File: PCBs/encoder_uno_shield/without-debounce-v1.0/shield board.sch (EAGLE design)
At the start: 13 parts, among them U1 ARDUINOR3-BPLACE

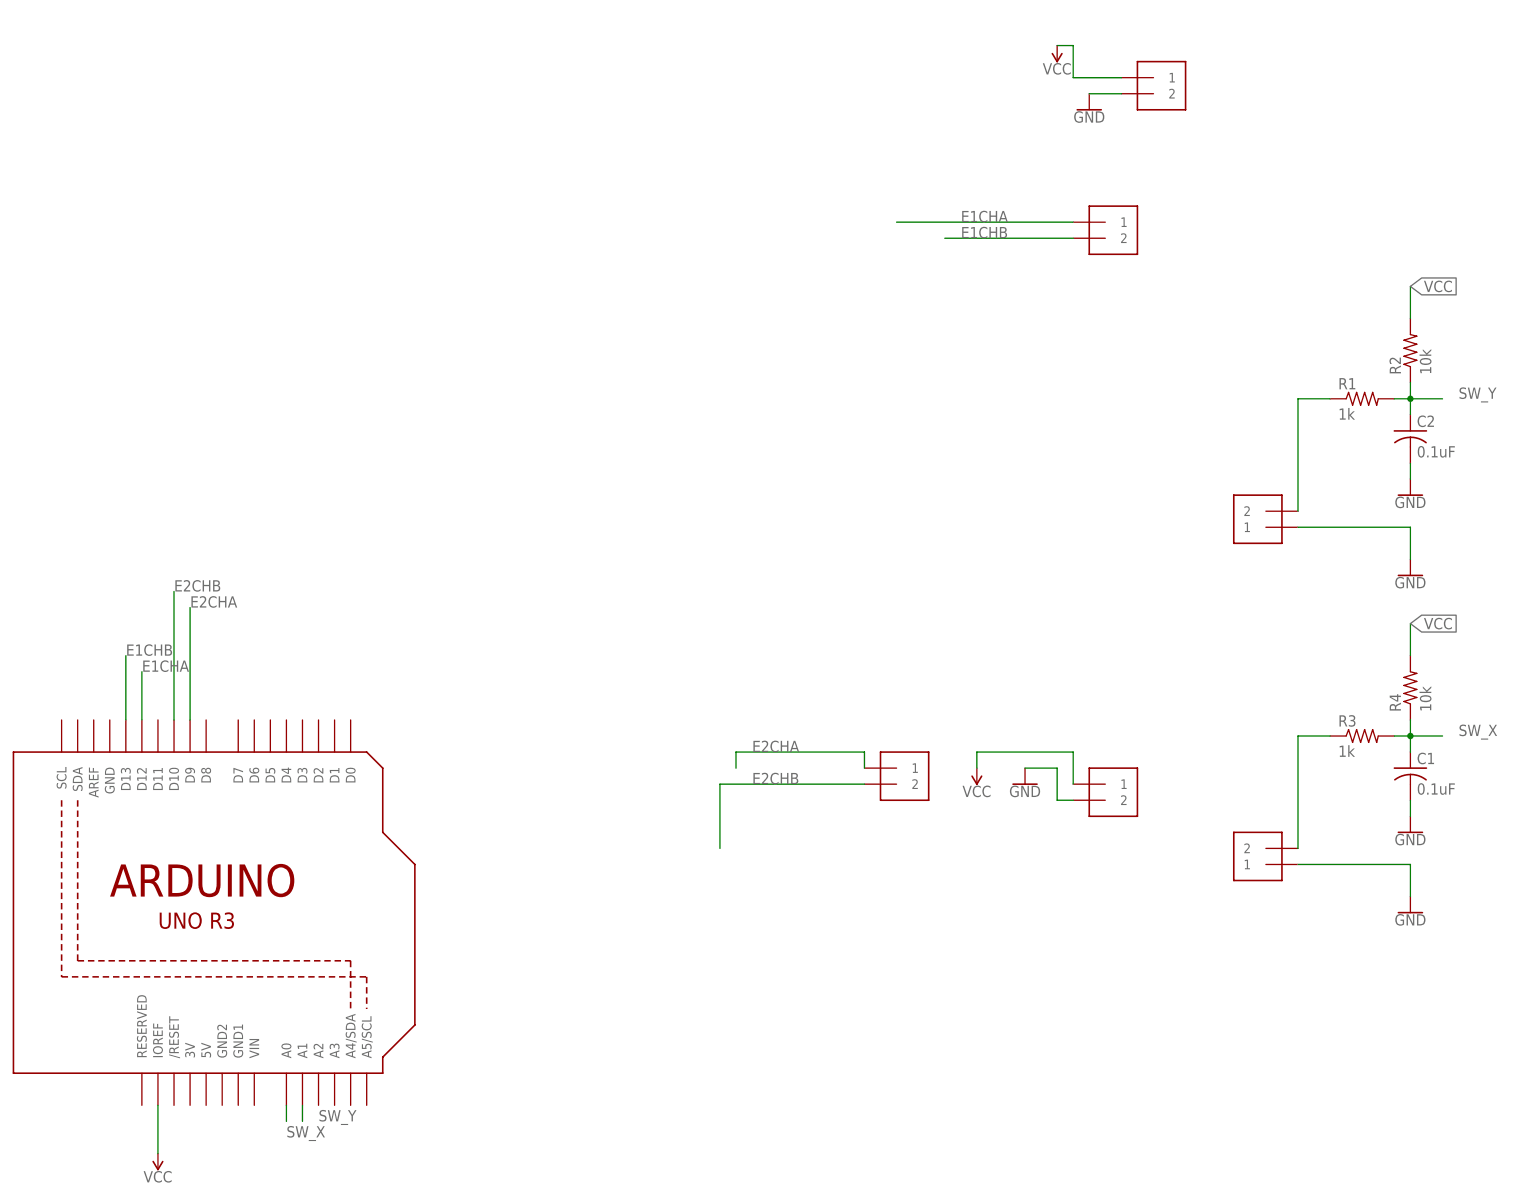
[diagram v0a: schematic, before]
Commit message: realized i only need one switch port, about to redesign
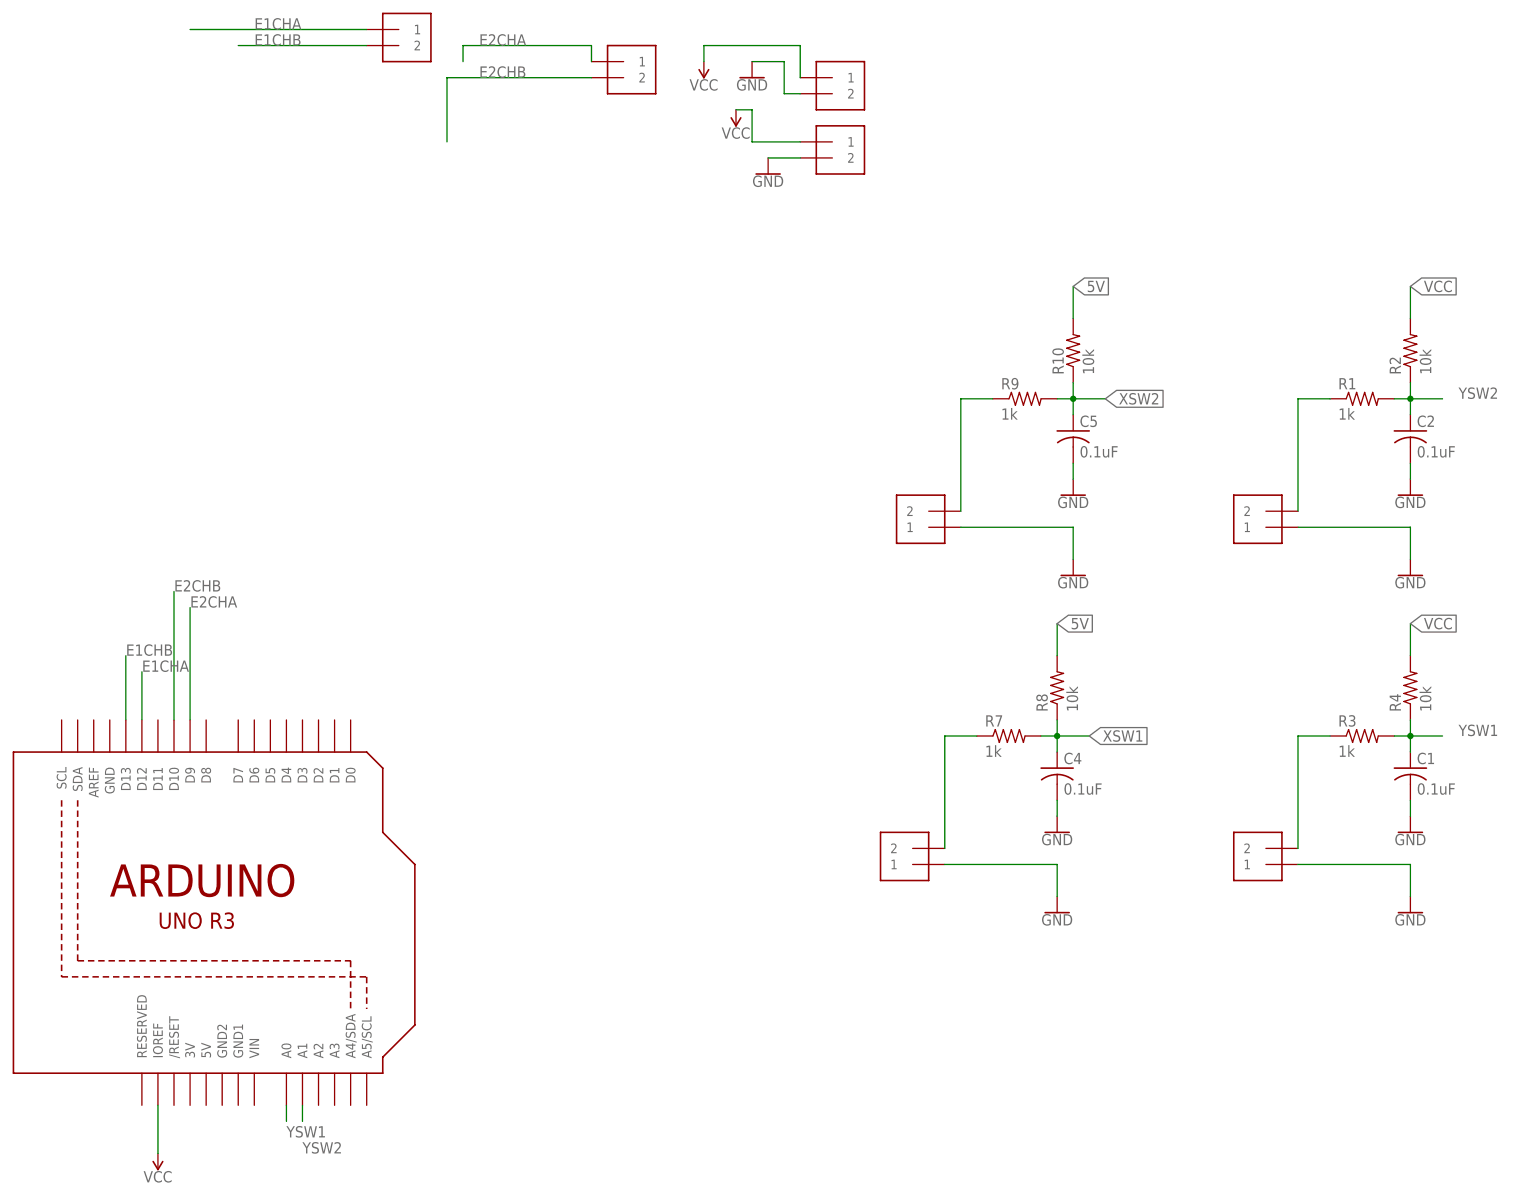
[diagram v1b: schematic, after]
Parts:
- added C4, C5: 0.1uF, adafruit:C-USC0603
- added R10, R8: 10k, resistor:R-US_R0603
- added R7, R9: 1k, resistor:R-US_R0603
- added U$7, U$8: MOLEX_0039301022, pat:MOLEX_0039301022
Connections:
- net SW_X renamed YSW1
- net SW_Y renamed YSW2
- new net 5V: R10.2, R8.2
- new net N$3: R7.1, U$7.2
- new net N$5: R9.1, U$8.2
- new net XSW1: C4.1, R7.2, R8.1
- new net XSW2: C5.1, R10.1, R9.2
- net GND: now also C4.2, C5.2, U$7.1, U$8.1

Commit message: routed new board design
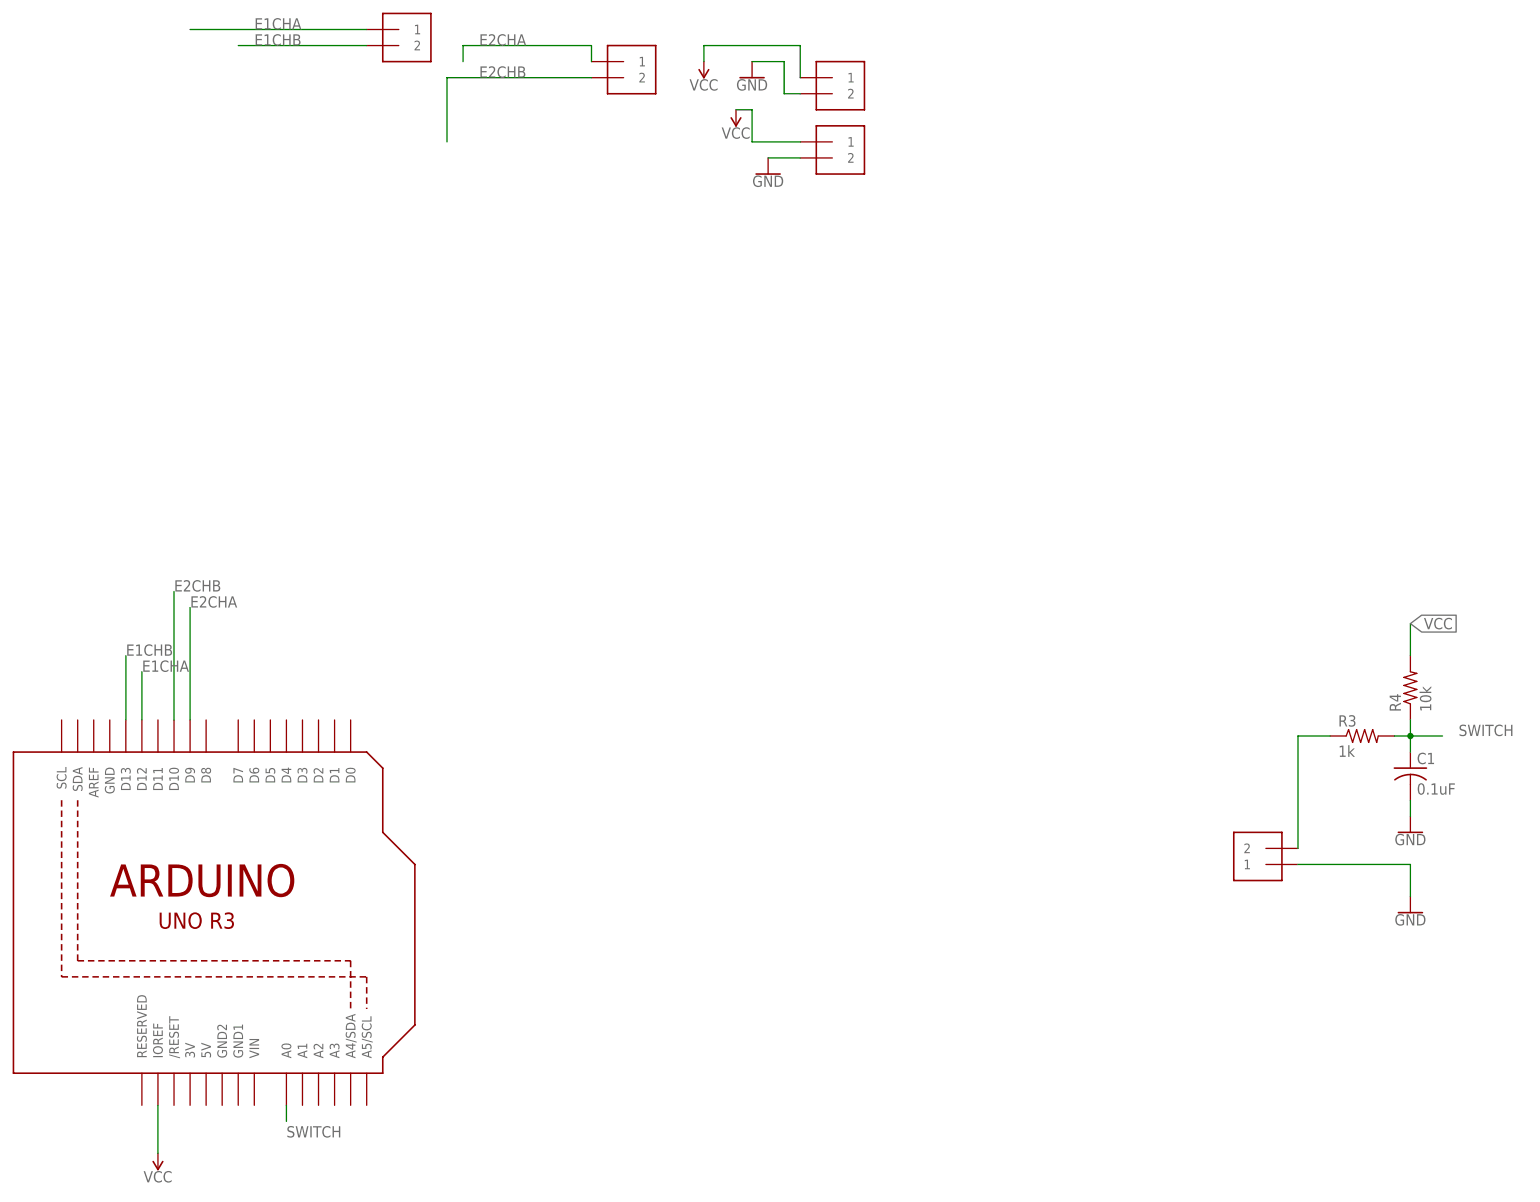
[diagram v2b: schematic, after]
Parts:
- removed C2, C4, C5: 0.1uF, adafruit:C-USC0603
- removed R1, R7, R9: 1k, resistor:R-US_R0603
- removed R10, R2, R8: 10k, resistor:R-US_R0603
- removed U$1, U$7, U$8: MOLEX_0039301022, pat:MOLEX_0039301022
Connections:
- net YSW1 renamed SWITCH
- removed net 5V: R10.2, R8.2
- removed net N$1: R1.1, U$1.2
- removed net N$3: R7.1, U$7.2
- removed net N$5: R9.1, U$8.2
- removed net XSW1: C4.1, R7.2, R8.1
- removed net XSW2: C5.1, R10.1, R9.2
- removed net YSW2: C2.1, R1.2, R2.1, U1.A1
- net GND: no longer C2.2, C4.2, C5.2, U$1.1, U$7.1, U$8.1
- net VCC: no longer R2.2
